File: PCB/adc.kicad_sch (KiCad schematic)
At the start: 2 parts, among them U12 ADS1115IDGS

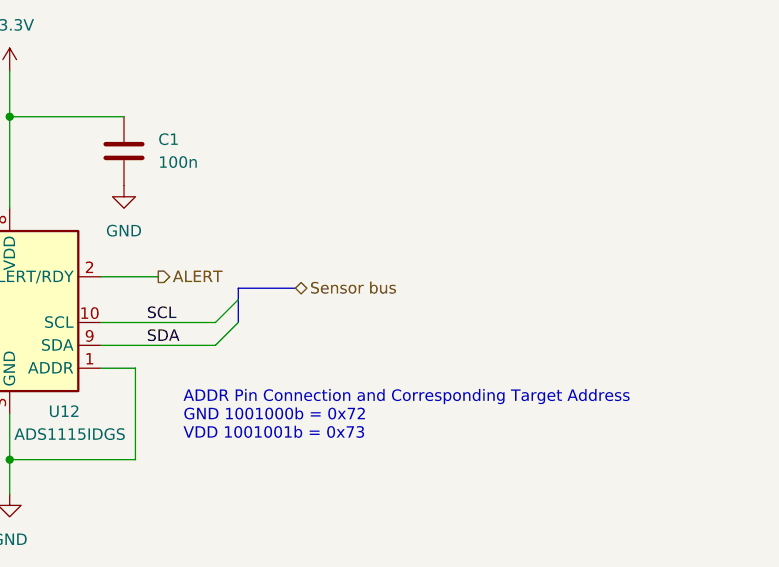
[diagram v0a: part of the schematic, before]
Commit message: removed usb port library
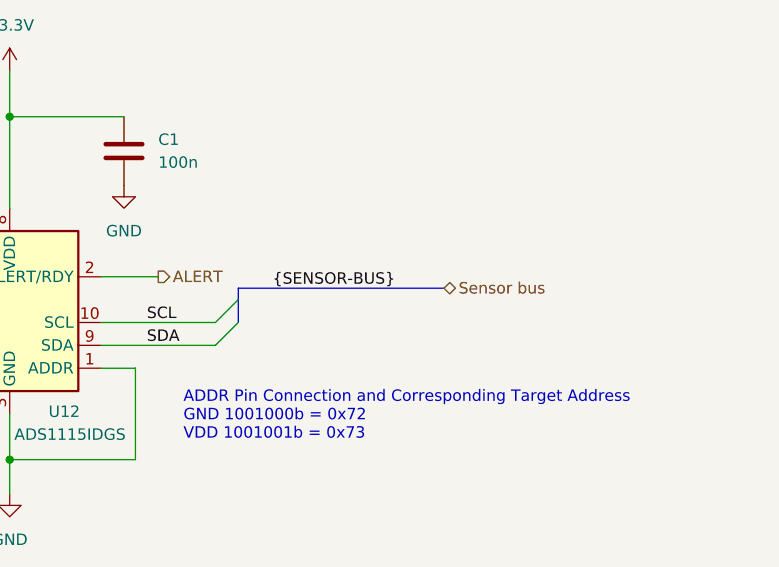
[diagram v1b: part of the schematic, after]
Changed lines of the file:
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@@
 	(bus
 		(pts
-			(xy 168.91 95.25) (xy 162.56 95.25)
+			(xy 185.42 95.25) (xy 162.56 95.25)
 		)
 		(stroke
@@
 		)
 	)
+	(label "{SENSOR-BUS}"
+		(at 166.37 95.25 0)
+		(effects
+			(font
+				(size 1.27 1.27)
+			)
+			(justify left bottom)
+		)
+	)
 	(label "SCL"
 		(at 152.4 99.06 0)
@@
 	(hierarchical_label "Sensor bus"
 		(shape bidirectional)
-		(at 168.91 95.25 0)
+		(at 185.42 95.25 0)
 		(effects
 			(font

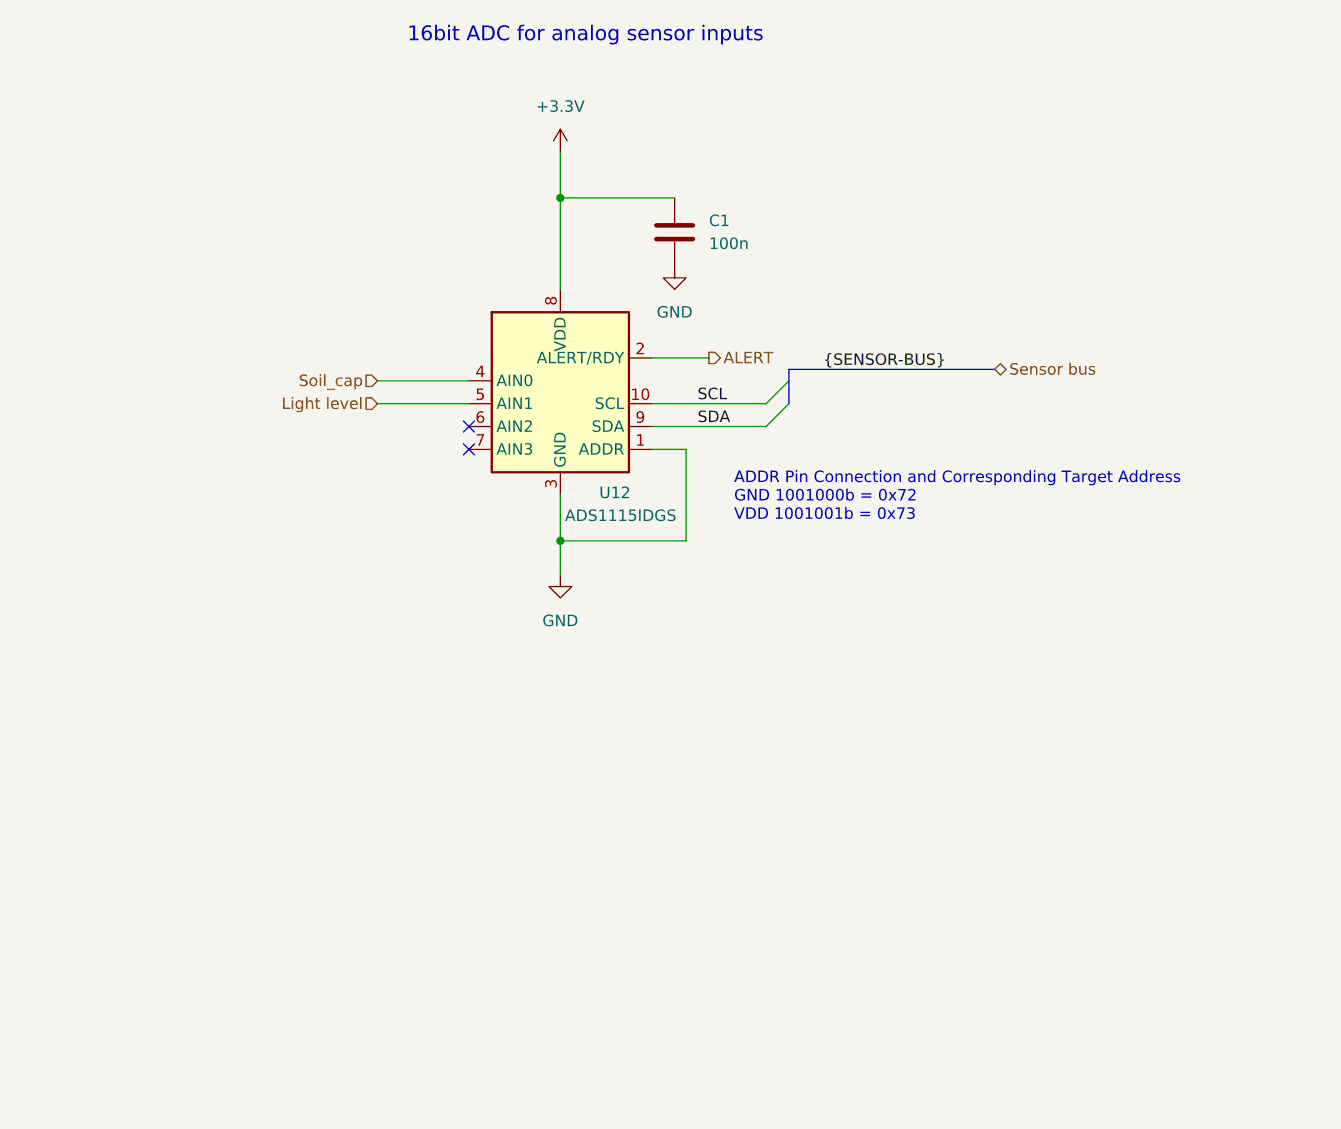
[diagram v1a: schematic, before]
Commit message: Optimized PCB lauout and added Header for LED indicator bar
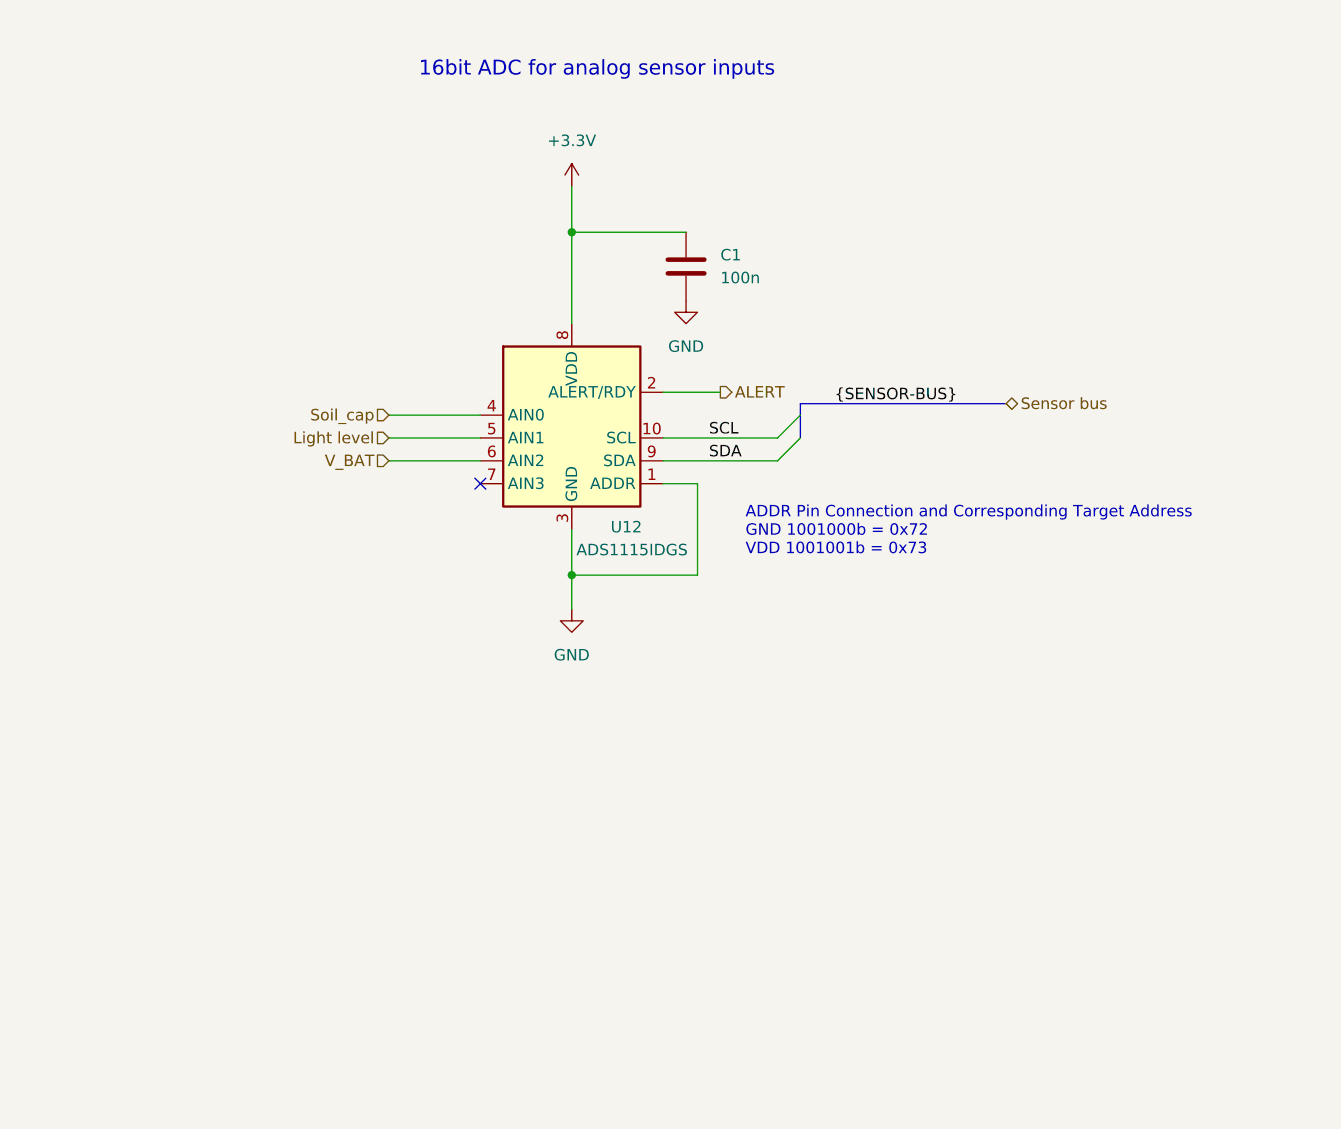
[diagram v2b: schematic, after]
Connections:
- net V_BAT: now reaches U12.6 (AIN2)
- no-connect marks 2 -> 1
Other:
- moved on the sheet: C1, U12

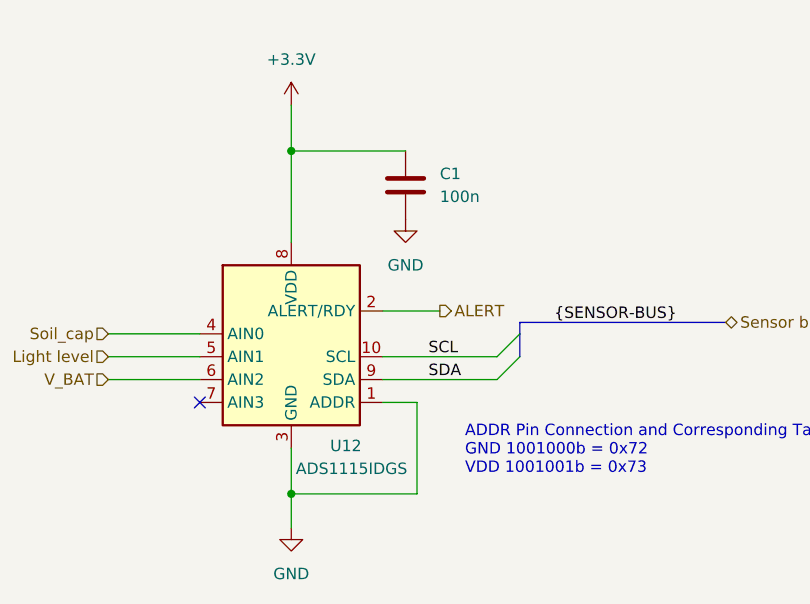
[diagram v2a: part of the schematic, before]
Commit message: Finished PCB routing and added reference designators
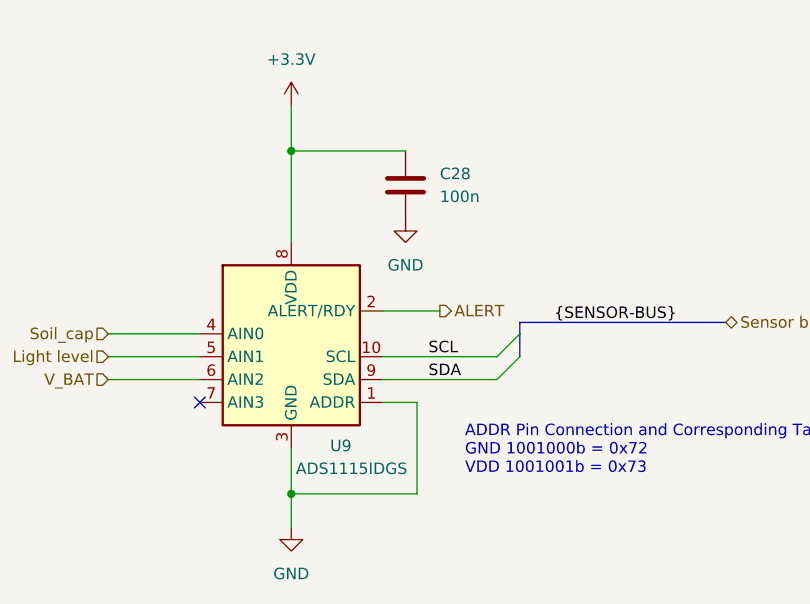
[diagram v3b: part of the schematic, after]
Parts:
- renumbered C1 to C28, U12 to U9
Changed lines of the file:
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@@
 		(dnp no)
 		(fields_autoplaced yes)
-		(property "Reference" "#PWR055"
+		(property "Reference" "#PWR058"
 			(at 151.13 93.98 0)
 			(effects
@@
 			(project ""
 				(path "/357055bf-c309-4d6b-a2fa-f5ee5ba59771/18c41965-930c-4295-847b-928f7d9a5c7f"
-					(reference "#PWR055")
+					(reference "#PWR058")
 					(unit 1)
 				)
@@
 		(dnp no)
 		(fields_autoplaced yes)
-		(property "Reference" "C1"
+		(property "Reference" "C28"
 			(at 154.94 82.5499 0)
 			(effects
@@
 			(project ""
 				(path "/357055bf-c309-4d6b-a2fa-f5ee5ba59771/18c41965-930c-4295-847b-928f7d9a5c7f"
-					(reference "C1")
+					(reference "C28")
 					(unit 1)
 				)
@@
 		(dnp no)
 		(fields_autoplaced yes)
-		(property "Reference" "#PWR05"
+		(property "Reference" "#PWR057"
 			(at 138.43 128.27 0)
 			(effects
@@
 			(project ""
 				(path "/357055bf-c309-4d6b-a2fa-f5ee5ba59771/18c41965-930c-4295-847b-928f7d9a5c7f"
-					(reference "#PWR05")
+					(reference "#PWR057")
 					(unit 1)
 				)
@@
 		(on_board yes)
 		(dnp no)
-		(property "Reference" "U12"
+		(property "Reference" "U9"
 			(at 142.748 112.776 0)
 			(effects
@@
 			(project "Plant-health-meter"
 				(path "/357055bf-c309-4d6b-a2fa-f5ee5ba59771/18c41965-930c-4295-847b-928f7d9a5c7f"
-					(reference "U12")
+					(reference "U9")
 					(unit 1)
 				)
@@
 		(dnp no)
 		(fields_autoplaced yes)
-		(property "Reference" "#PWR050"
+		(property "Reference" "#PWR056"
 			(at 138.43 78.74 0)
 			(effects
@@
 			(project ""
 				(path "/357055bf-c309-4d6b-a2fa-f5ee5ba59771/18c41965-930c-4295-847b-928f7d9a5c7f"
-					(reference "#PWR050")
-					(unit 1)
-				)
+					(reference "#PWR056")
+					(unit 1)
+				)

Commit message: Final touches to PCB
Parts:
- added R25, R26: 10k, Resistor_SMD:R_0402_1005Metric, symbol Device:R
- renumbered C28 to C30
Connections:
- net GND: now also R26.1
- net V_BAT: now also R25.1; no longer U9.6 (AIN2)
- new net: R25.2, R26.2, U9.6 (AIN2)
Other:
- note added: "Divide battery voltage in half max: 4.0 / 2 = 2.0"

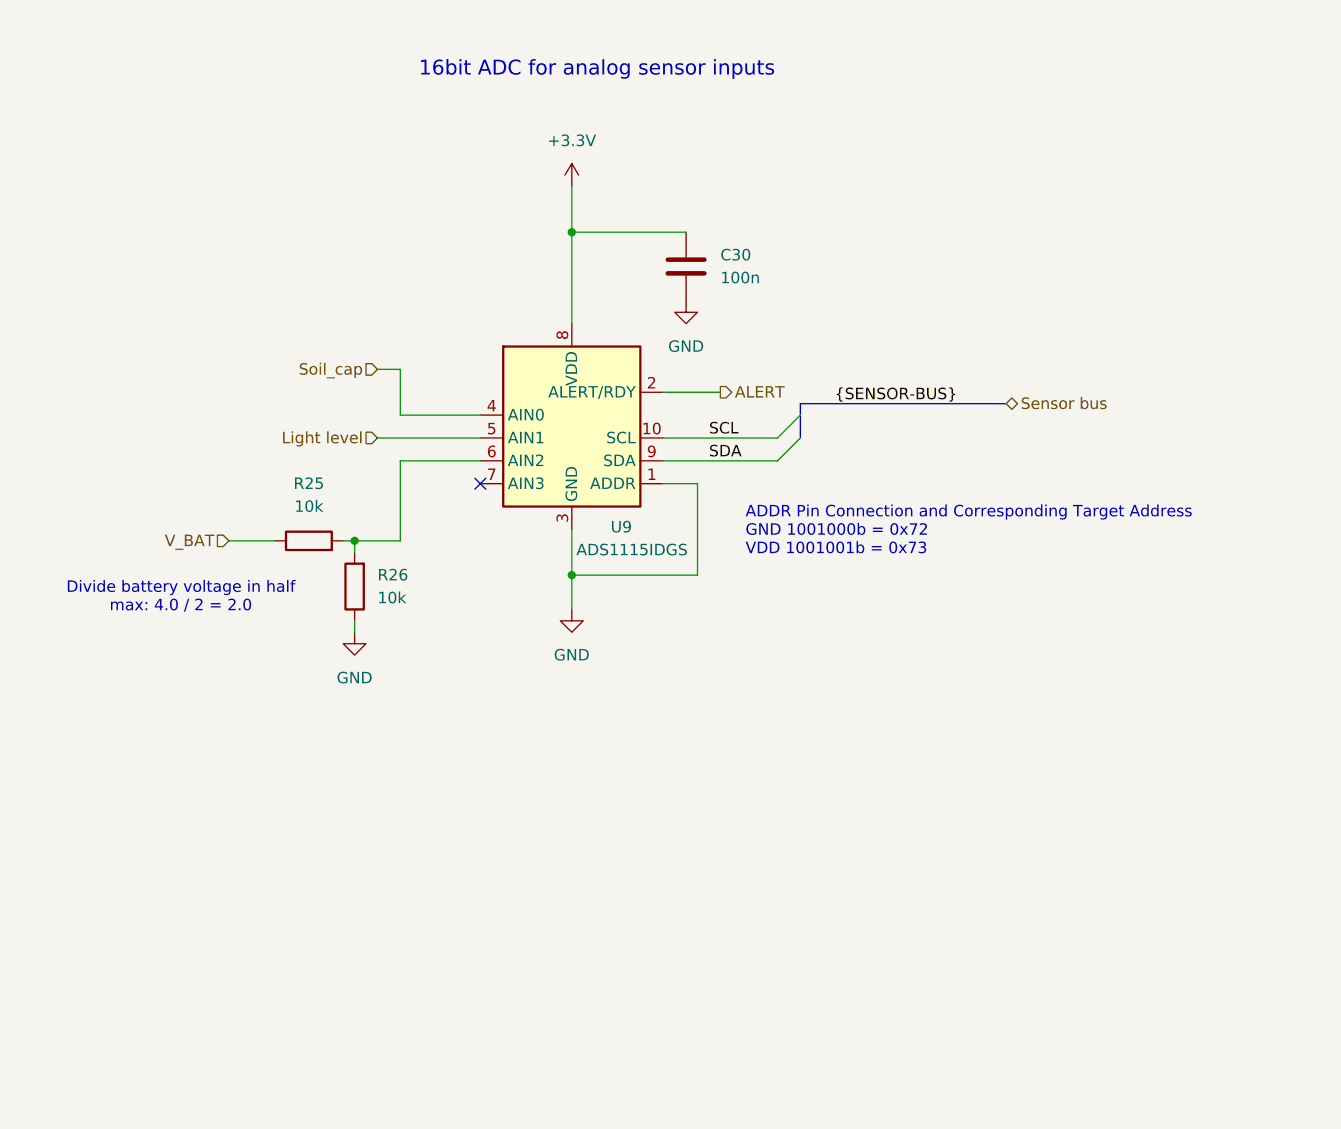
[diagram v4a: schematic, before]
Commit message: ESD protection and Boost UVLO
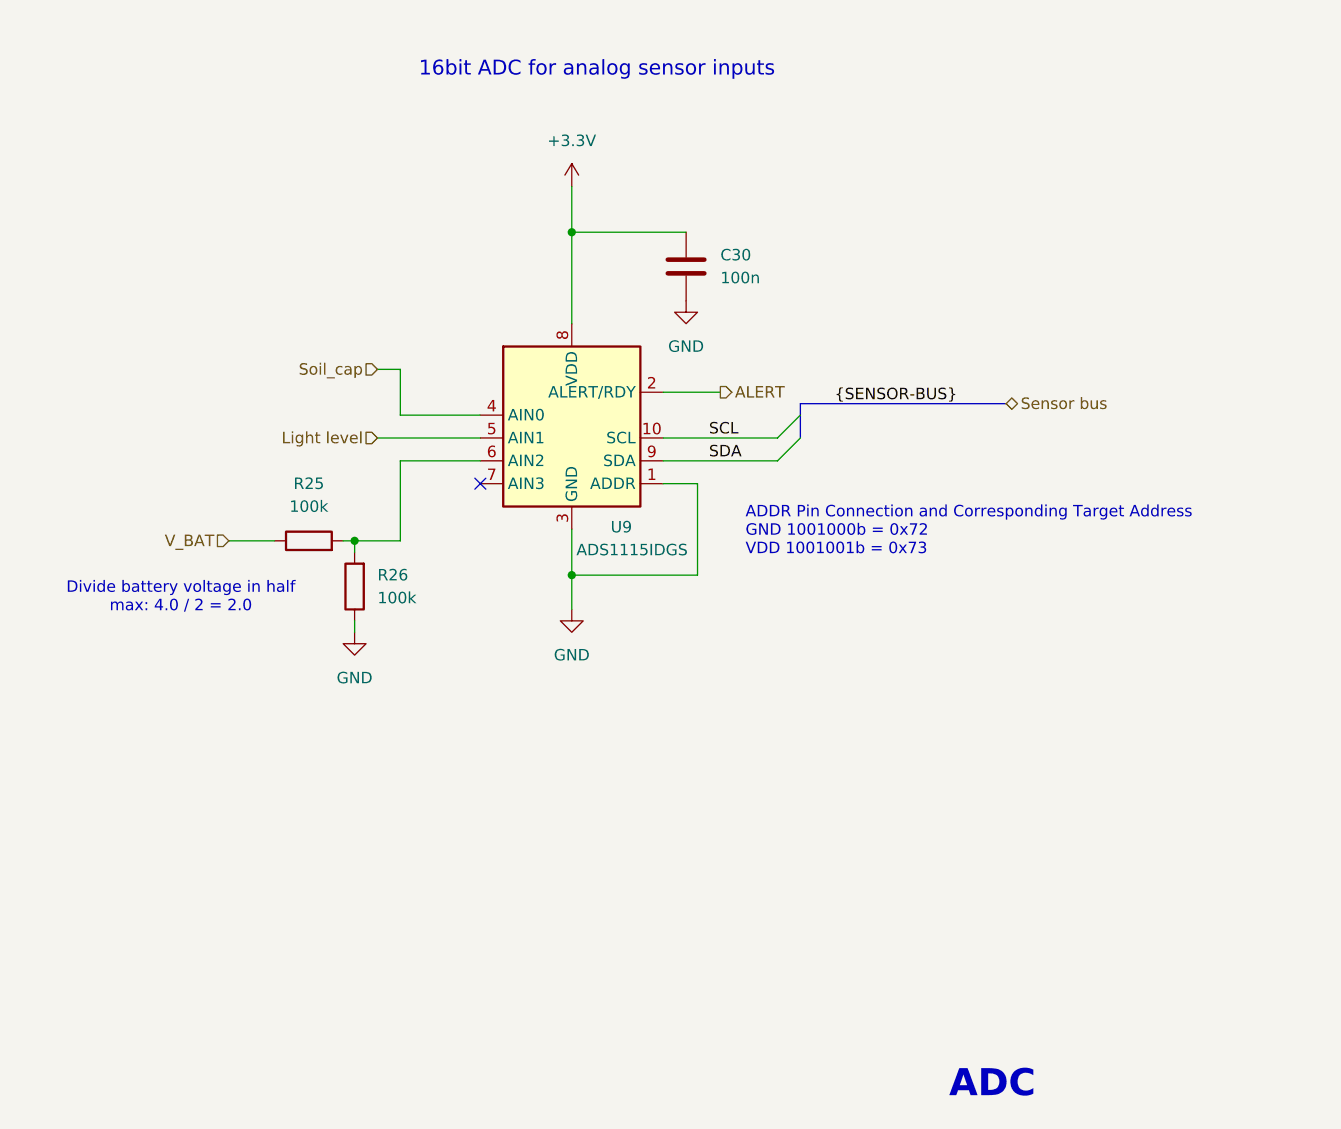
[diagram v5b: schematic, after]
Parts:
- R25, R26: value 10k -> 100k
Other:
- note added: "ADC"
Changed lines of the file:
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@@
+		)
+	)
+	(text "ADC"
+		(exclude_from_sim no)
+		(at 185.166 174.752 0)
+		(effects
+			(font
+				(size 3 3)
+				(thickness 0.6)
+				(bold yes)
+			)
 		)
 	)
@@
 			)
 		)
-		(property "Value" "10k"
+		(property "Value" "100k"
 			(at 116.84 120.6499 0)
 			(effects
@@
 			)
 		)
-		(property "Value" "10k"
+		(property "Value" "100k"
 			(at 109.22 110.49 90)
 			(effects

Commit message: Production files
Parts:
- renumbered R25 to R23, R26 to R24
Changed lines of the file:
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@@
 		(dnp no)
 		(fields_autoplaced yes)
-		(property "Reference" "#PWR059"
+		(property "Reference" "#PWR058"
 			(at 151.13 93.98 0)
 			(effects
@@
 			(project ""
 				(path "/357055bf-c309-4d6b-a2fa-f5ee5ba59771/18c41965-930c-4295-847b-928f7d9a5c7f"
-					(reference "#PWR059")
+					(reference "#PWR058")
 					(unit 1)
 				)
@@
 		(dnp no)
 		(fields_autoplaced yes)
-		(property "Reference" "R26"
+		(property "Reference" "R24"
 			(at 116.84 118.1099 0)
 			(effects
@@
 			(project "Plant-health-meter"
 				(path "/357055bf-c309-4d6b-a2fa-f5ee5ba59771/18c41965-930c-4295-847b-928f7d9a5c7f"
-					(reference "R26")
+					(reference "R24")
 					(unit 1)
 				)
@@
 		(dnp no)
 		(fields_autoplaced yes)
-		(property "Reference" "#PWR058"
+		(property "Reference" "#PWR057"
 			(at 138.43 128.27 0)
 			(effects
@@
 			(project ""
 				(path "/357055bf-c309-4d6b-a2fa-f5ee5ba59771/18c41965-930c-4295-847b-928f7d9a5c7f"
-					(reference "#PWR058")
+					(reference "#PWR057")
 					(unit 1)
 				)
@@
 		(dnp no)
 		(fields_autoplaced yes)
-		(property "Reference" "#PWR057"
+		(property "Reference" "#PWR056"
 			(at 138.43 78.74 0)
 			(effects
@@
 			(project ""
 				(path "/357055bf-c309-4d6b-a2fa-f5ee5ba59771/18c41965-930c-4295-847b-928f7d9a5c7f"
-					(reference "#PWR057")
+					(reference "#PWR056")
 					(unit 1)
 				)
@@
 		(dnp no)
 		(fields_autoplaced yes)
-		(property "Reference" "R25"
+		(property "Reference" "R23"
 			(at 109.22 107.95 90)
 			(effects
@@
 			(project ""
 				(path "/357055bf-c309-4d6b-a2fa-f5ee5ba59771/18c41965-930c-4295-847b-928f7d9a5c7f"
-					(reference "R25")
+					(reference "R23")
 					(unit 1)
 				)
@@
 		(dnp no)
 		(fields_autoplaced yes)
-		(property "Reference" "#PWR056"
+		(property "Reference" "#PWR055"
 			(at 114.3 130.81 0)
 			(effects
@@
 			(project ""
 				(path "/357055bf-c309-4d6b-a2fa-f5ee5ba59771/18c41965-930c-4295-847b-928f7d9a5c7f"
-					(reference "#PWR056")
-					(unit 1)
-				)
+					(reference "#PWR055")
+					(unit 1)
+				)
